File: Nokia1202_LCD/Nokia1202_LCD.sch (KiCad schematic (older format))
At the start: 5 parts, among them P1 CONN_01X08

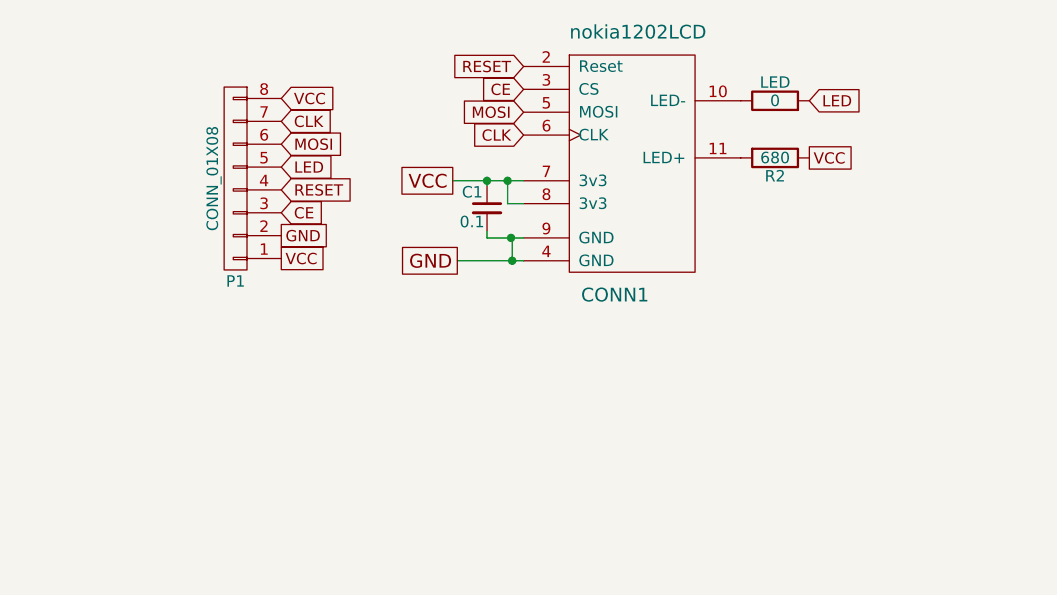
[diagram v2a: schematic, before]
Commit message: Too many untracked changes: LCD boards update and switch to KiCAD version 5
Update the Nokia LCD breakout boards
Add more KiCAD simulation projects
Update most projects to KiCAD version 5
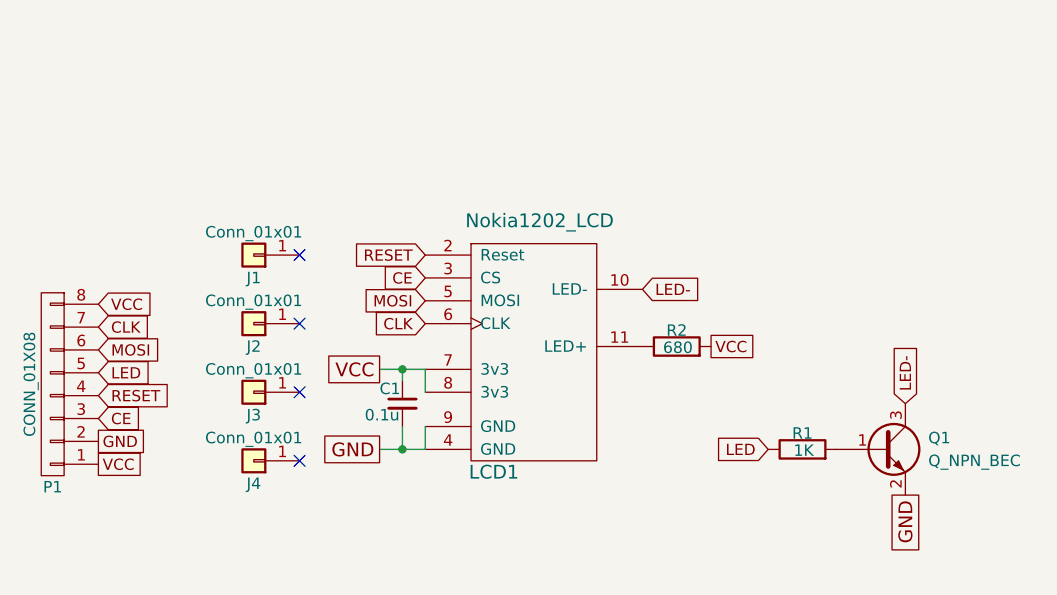
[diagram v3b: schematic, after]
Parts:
- removed CONN1: nokia1202LCD, Connect:Nokia1202LCD, symbol Nokia1202_LCD-rescue:nokia1202LCD-RESCUE-Nokia1202_LCD
- removed LED: 0, Resistors_SMD:R_1206, symbol device:R
- added J1, J2, J3, J4: Conn_01x01, Pin_Headers:Pin_Header_Angled_1x01_Pitch2.54mm, symbol Conn_01x01
- added LCD1: Nokia1202_LCD, Displays:Nokia1202LCD_folded, symbol Nokia1202_LCD-rescue:nokia1202LCD-RESCUE-Nokia1202_LCD
- added Q1: Q_NPN_BEC, TO_SOT_Packages_SMD:SOT-23, symbol Q_NPN_BEC
- added R1: 1K, Resistors_SMD:R_0805, symbol device:R
- C1: value 0.1 -> 0.1u; footprint Capacitors_SMD:C_1206 -> Capacitors_Tantalum_SMD:CP_Tantalum_Case-A_EIA-3216-18_Wave
- R2: footprint Resistors_SMD:R_1206 -> Resistors_SMD:R_0805
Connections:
- net CE: now also LCD1.3 (CS)
- net CLK: now also LCD1.6 (CLK)
- net GND: now also LCD1.4 (GND), LCD1.9 (GND), Q1.2 (E)
- net LED: now also R1.1
- net MOSI: now also LCD1.5 (MOSI)
- net RESET: now also LCD1.2 (Reset)
- net VCC: now also R2.2, LCD1.7 (3v3), LCD1.8 (3v3); no longer R2.1
- new net: LCD1.11 (LED+), R2.1
- new net: Q1.1 (B), R1.2
- new net LED-: LCD1.10 (LED-), Q1.3 (C)
- no-connect marks 0 -> 4
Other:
- moved on the sheet: P1
